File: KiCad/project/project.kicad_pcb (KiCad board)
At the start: 4 copper layers, 26.1 x 21 mm, 20 parts, among them P1 Header-Female-2.54_1x3, U1 DRV8313PWPR

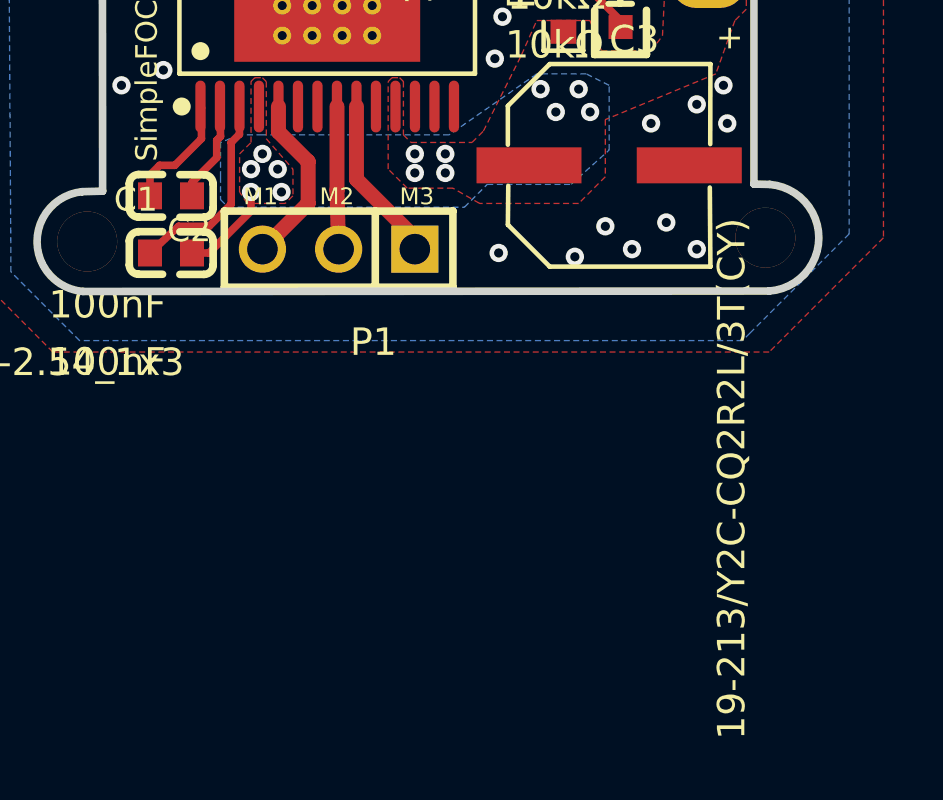
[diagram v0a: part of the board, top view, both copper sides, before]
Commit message: PCB: add C5 footprint, widen VM trace to 0.8mm
- Added C5 (clone of C3, netted VCC/GND), parked below the board outline
  pending placement (shows as 2 ratsnest until routed).
- Widened the VM/VCC trace 0.254 -> 0.8mm (Power-class). No shorts.
- Phase traces left at 0.5mm: widening to 0.8mm shorts U1_8<->U1_9 at the
  0.65mm-pitch HTSSOP escape (they must neck at the IC, a routing task).
  0.5mm carries 1.5A.

DRC: 0 shorting_items, 2 unconnected (C5's pads). Remaining are
pre-existing import artifacts. Footprint resizes + P1 terminal block +
routing belong to the re-layout (they need the larger board).

Co-Authored-By: Claude Opus 4.8 <noreply@anthropic.com>
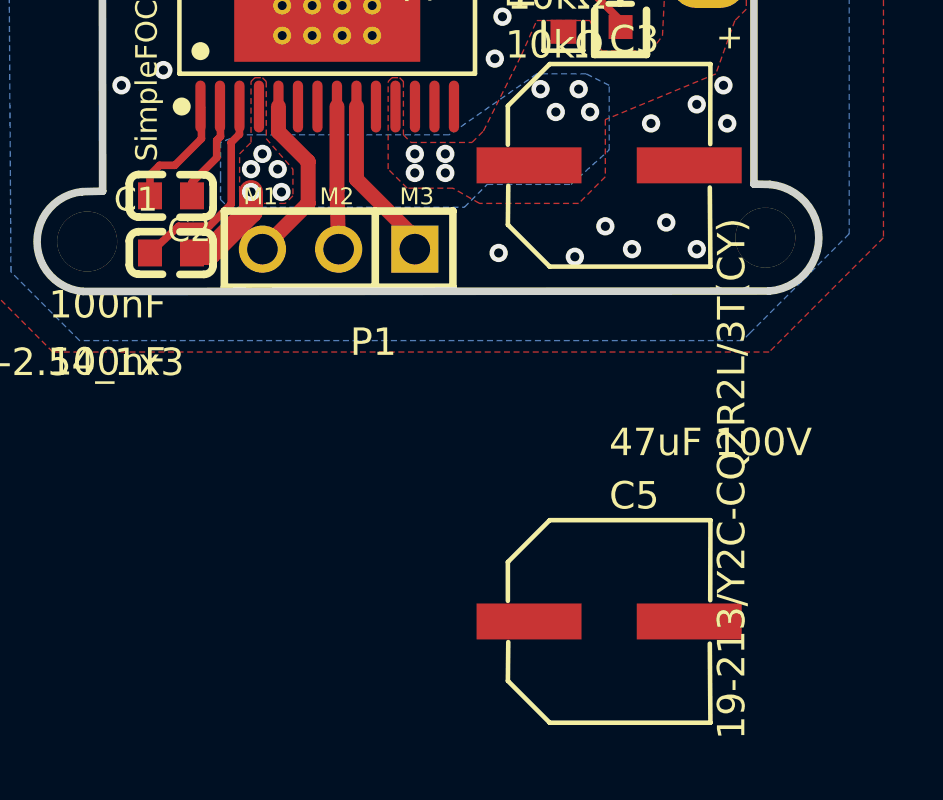
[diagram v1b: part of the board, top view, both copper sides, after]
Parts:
- added C5: 47uF 100V, CAP-SMD_BD6.3-L6.6-W6.6-FD, F.Cu at (153.0, 124.0)

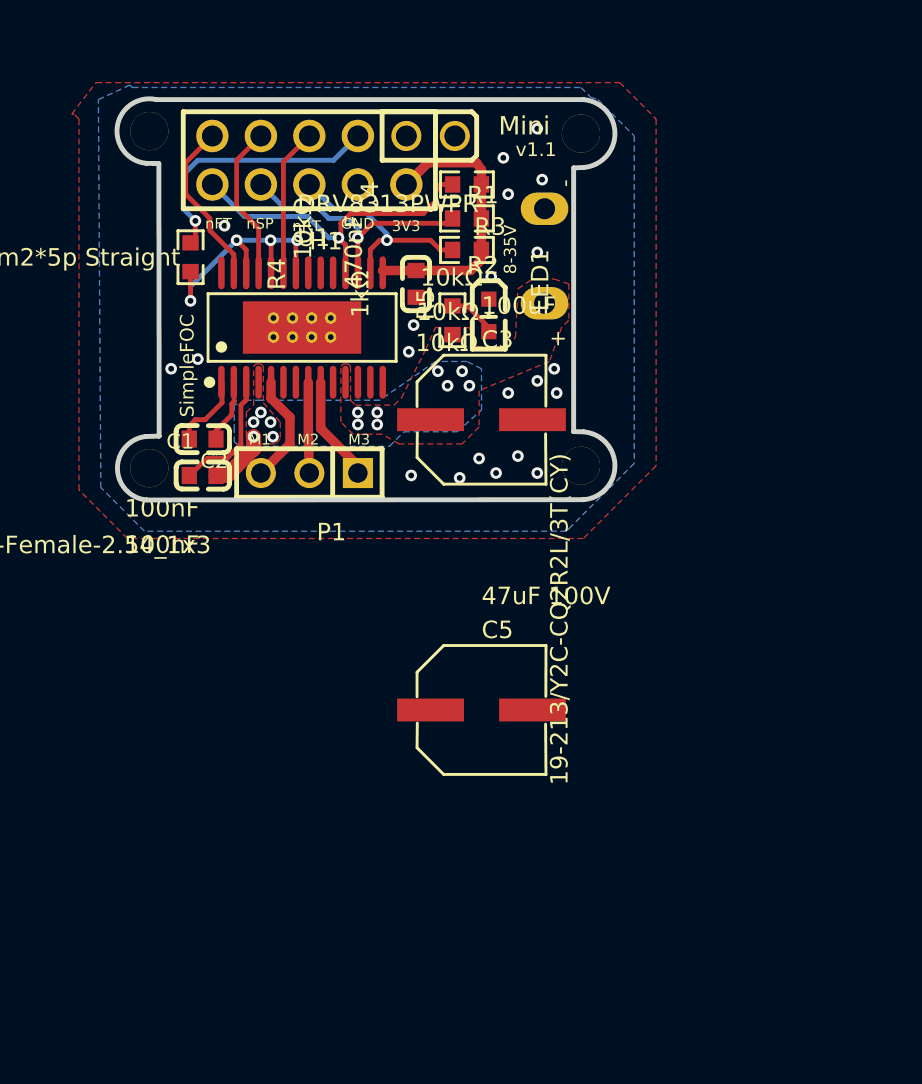
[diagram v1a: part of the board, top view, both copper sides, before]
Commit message: PCB: round corners, add M3 corner holes + missing TB_PWR1 footprint
Continuing the 40x40 mm re-layout (step 1):
- Edge.Cuts: 3 mm rounded corners (4 segments + 4 fillet arcs).
- Add MH1-MH4 (MountingHole_3.2mm_M3, NPTH) at the corners, symmetric
  32x32 mm pattern (4 mm inset). MH1 overlaps H1 until H1 is moved.
- Add TB_PWR1 footprint (was in the schematic but the import never laid
  it out): TerminalBlock_MaiXu_MX126-5.0-02P, pad1->GND, pad2->VCC,
  parked off-board pending placement.
- Re-pour zones after the edge change (clears stale-fill edge flags).

DRC: 228 violations, 0 shorting_items, 4 unconnected (C5 + TB_PWR1).
The 7 Pad_gge* orphans (old 2 mm GND mounting holes + original power
pads) are now superseded by MH1-4 / TB_PWR1 -- flagged in docs for
deletion during GUI placement.

Co-Authored-By: Claude Opus 4.8 (1M context) <noreply@anthropic.com>
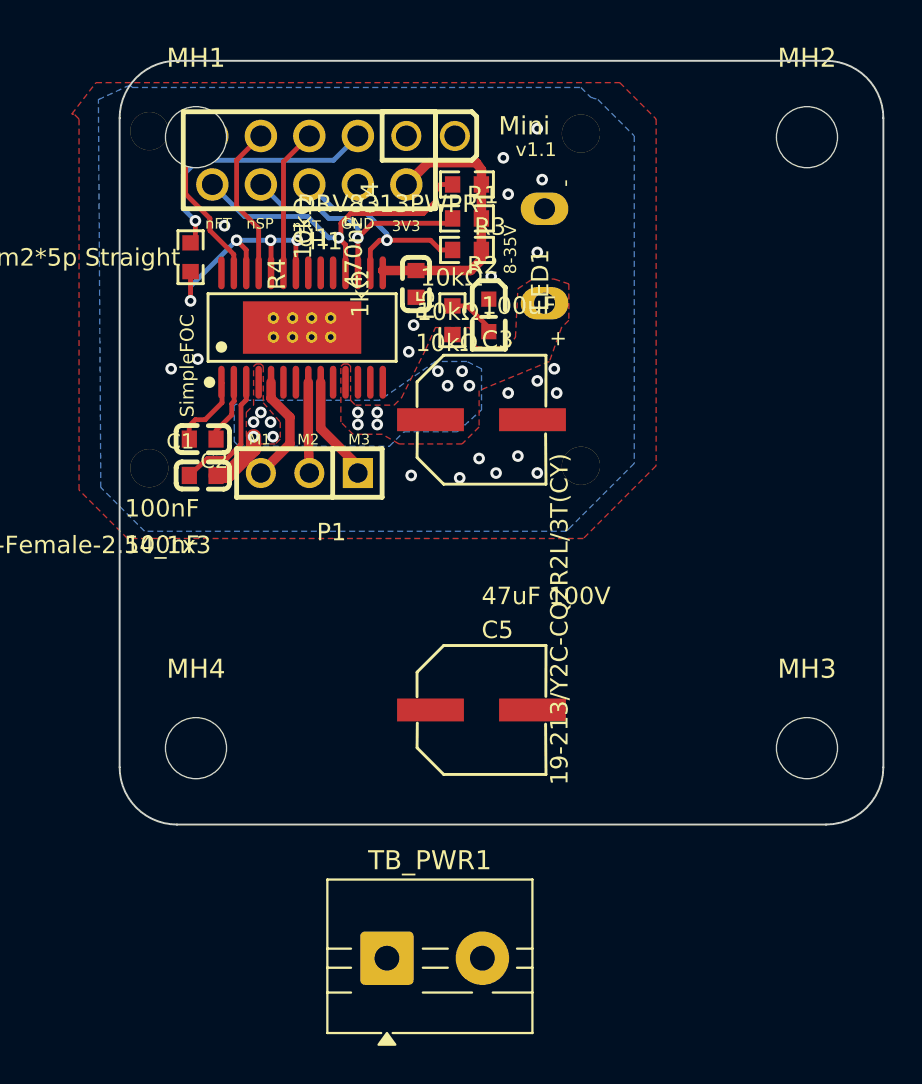
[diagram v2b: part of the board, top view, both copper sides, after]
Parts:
- added MH1: MountingHole_3.2mm_M3, MountingHole_3.2mm_M3, F.Cu at (138.0, 94.0)
- added MH2: MountingHole_3.2mm_M3, MountingHole_3.2mm_M3, F.Cu at (170.0, 94.0)
- added MH3: MountingHole_3.2mm_M3, MountingHole_3.2mm_M3, F.Cu at (170.0, 126.0)
- added MH4: MountingHole_3.2mm_M3, MountingHole_3.2mm_M3, F.Cu at (138.0, 126.0)
- added TB_PWR1: TB002-500-02BE, TerminalBlock_MaiXu_MX126-5.0-02P_1x02_P5.00mm, F.Cu at (148.0, 137.0)
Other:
- board size 26.1 x 21 mm -> 40 x 40 mm

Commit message: PCB: clear routing/zones/orphans for tool-driven re-place + re-route
Hand a clean board to KiCadRoutingTools: removed all 112 tracks + 42 vias,
the 7 Pad_gge import orphans (4 old corner mounting holes + 3 old power-input
pads, both superseded by MH1-MH4 / TB_PWR1), all 7 stale copper zones, and the
Dwgs.User documentation graphics. Kept all real components, MH1-MH4, and the
40x40 Edge.Cuts outline. Planes will be regenerated via route_planes.

Co-Authored-By: Claude Opus 4.8 (1M context) <noreply@anthropic.com>
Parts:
- removed Pad_gge5124: Pad_gge5124, Pad_gge5124
- removed Pad_gge5154: Pad_gge5154, Pad_gge5154
- removed Pad_gge5250: Pad_gge5250, Pad_gge5250
- removed Pad_gge5325: Pad_gge5325, Pad_gge5325
- removed Pad_gge5349: Pad_gge5349, Pad_gge5349
- removed Pad_gge7437: Pad_gge7437, Pad_gge7437
- removed Pad_gge9415: Pad_gge9415, Pad_gge9415
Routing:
- net NFLT: track 17.6 -> 0.00 mm, vias 1 -> 0
- net 3.3V: track 14.7 -> 0.00 mm
- net EN: track 14.3 -> 0.00 mm, vias 4 -> 0
- net R4_1: track 14.1 -> 0.00 mm, vias 1 -> 0
- net NSLP: track 13.8 -> 0.00 mm, vias 1 -> 0
- net NRES: track 11.4 -> 0.00 mm, vias 1 -> 0
- net IN1: track 8.79 -> 0.00 mm
- net U1_25: track 8.17 -> 0.00 mm
- net IN3: track 7.73 -> 0.00 mm
- net U1_3: track 6.73 -> 0.00 mm
- net U1_5: track 5.80 -> 0.00 mm
- net U1_9: track 5.56 -> 0.00 mm
- net U1_8: track 4.76 -> 0.00 mm
- net U1_1: track 4.00 -> 0.00 mm
- net U1_2: track 3.37 -> 0.00 mm
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- removed copper zone on B.Cu, net GND
- removed copper zone on F.Cu, net GND
- removed copper zone on In1.Cu, net GND
- removed copper zone on In2.Cu, net GND
- removed copper zone on B.Cu, net VCC
- removed copper zone on F.Cu, net VCC

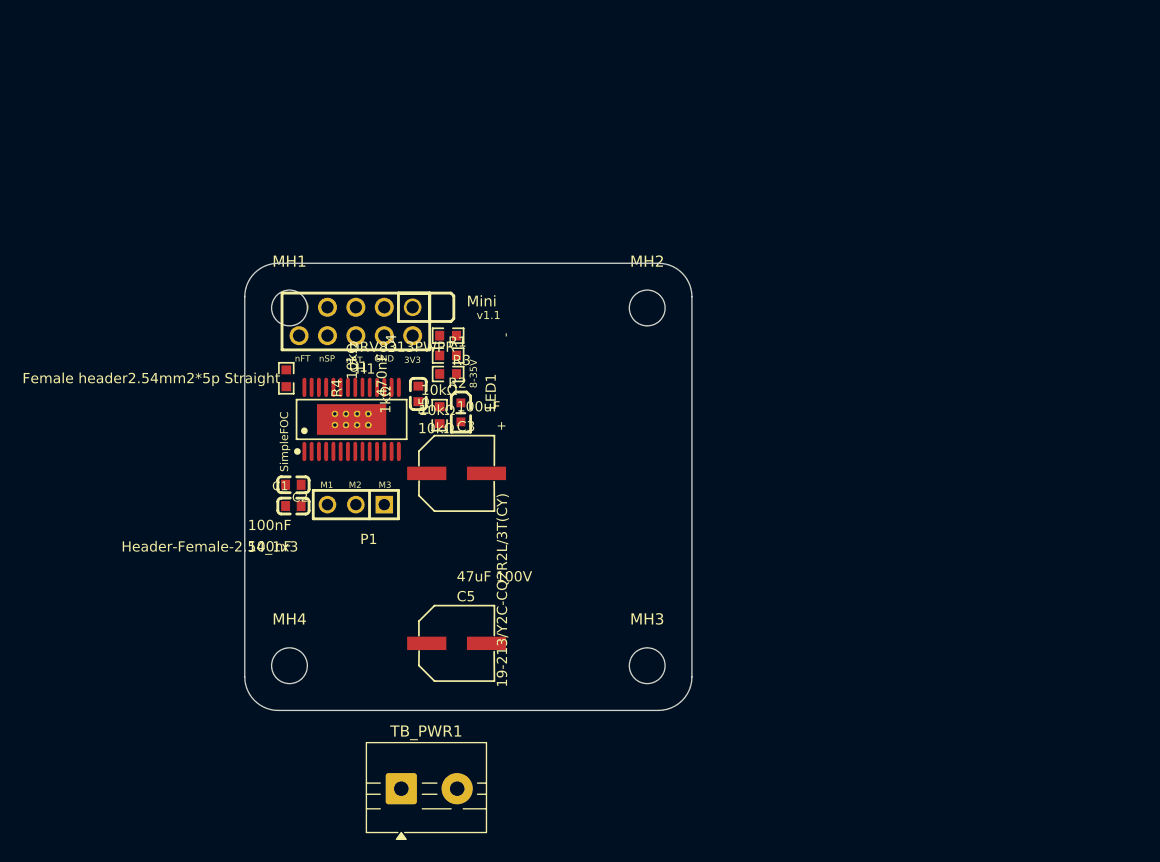
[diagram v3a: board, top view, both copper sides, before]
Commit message: PCB: first-pass macro placement on 40x40 board
Power-in (TB_PWR1) left edge, motor-out (P1) right edge, control header (H1)
top edge facing U1's logic row. U1 central; bulk VM cans in the open bottom
area; CP/bypass caps under the power row; logic pulls between H1 and U1; LED
by the 3.3V pin. 0 courtyard overlaps (remaining DRC = cosmetic silk +
unrouted ratsnest). Starting point for KiCadRoutingTools polish + route.

Co-Authored-By: Claude Opus 4.8 (1M context) <noreply@anthropic.com>
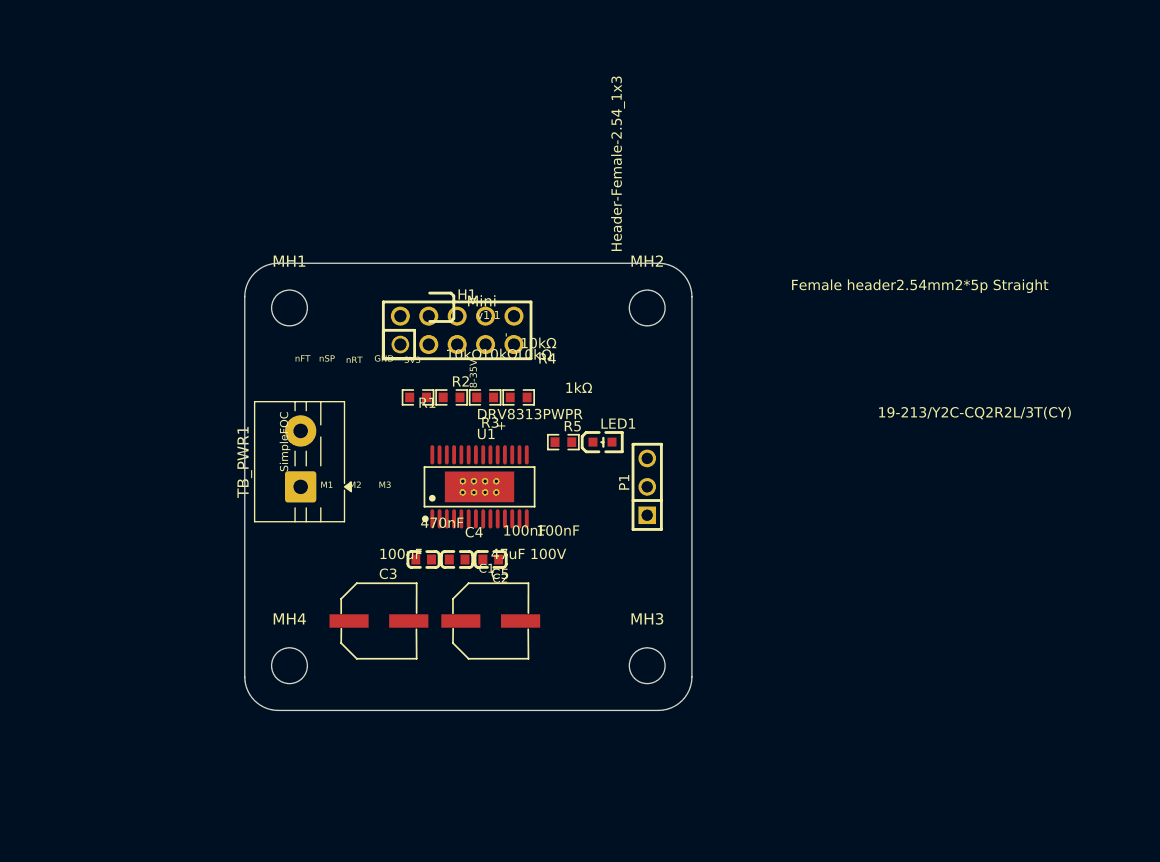
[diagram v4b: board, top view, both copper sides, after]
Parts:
- moved TB_PWR1 28.5 mm to (139.0, 110.0), turned to 90 degrees
- moved P1 26.1 mm to (170.0, 110.0), turned to 90 degrees
- moved R4 20.9 mm to (158.5, 102.0), turned to 0 degrees
- moved C2 18.3 mm to (156.0, 116.5), turned to 0 degrees
- moved C1 16.1 mm to (153.0, 116.5), turned to 0 degrees
- moved C3 14.9 mm to (146.0, 122.0)
- moved C4 14.8 mm to (150.0, 116.5), turned to 0 degrees
- moved LED1 12.9 mm to (166.0, 106.0), turned to 0 degrees
- moved U1 12.9 mm to (155.0, 110.0)
- moved R5 11.3 mm to (162.5, 106.0), turned to 0 degrees
- moved H1 9.10 mm to (153.0, 96.0), turned to 0 degrees
- moved R1 6.14 mm to (149.5, 102.0), turned to 0 degrees
- moved R3 3.92 mm to (155.5, 102.0), turned to 0 degrees
- moved R2 3.76 mm to (152.5, 102.0), turned to 0 degrees
- moved C5 3.64 mm to (156.0, 122.0)

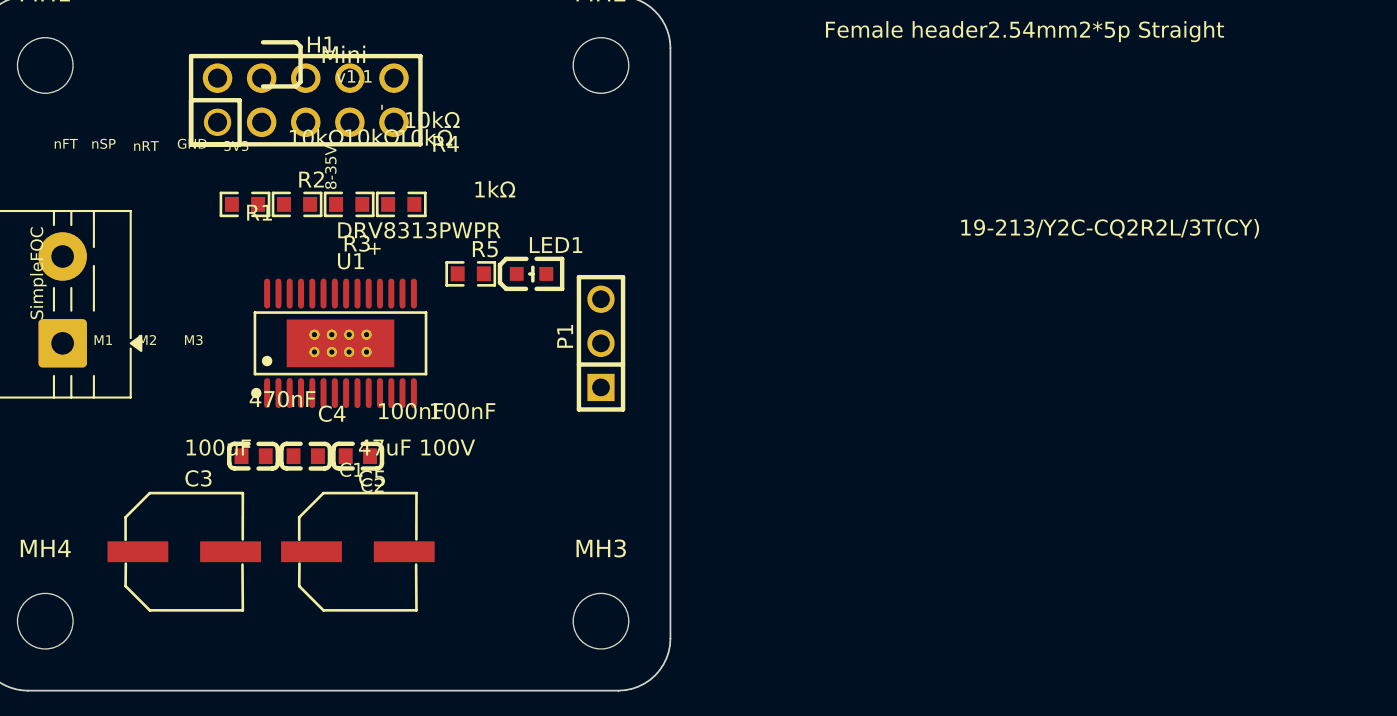
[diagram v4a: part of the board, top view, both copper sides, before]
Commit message: PCB: place_optimize polish of macro placement
KiCadRoutingTools place_optimize (connectors/U1/holes locked): airwire
194.9->179.9mm, crossings 39->19, 10 small parts nudged. Bulk cans manually
reset clear of MH4 afterward. 0 courtyard overlaps. Writer verified to
preserve the 4-layer stackup (GND1/GND2 inner names intact), 19 footprints,
20 nets.

Co-Authored-By: Claude Opus 4.8 (1M context) <noreply@anthropic.com>
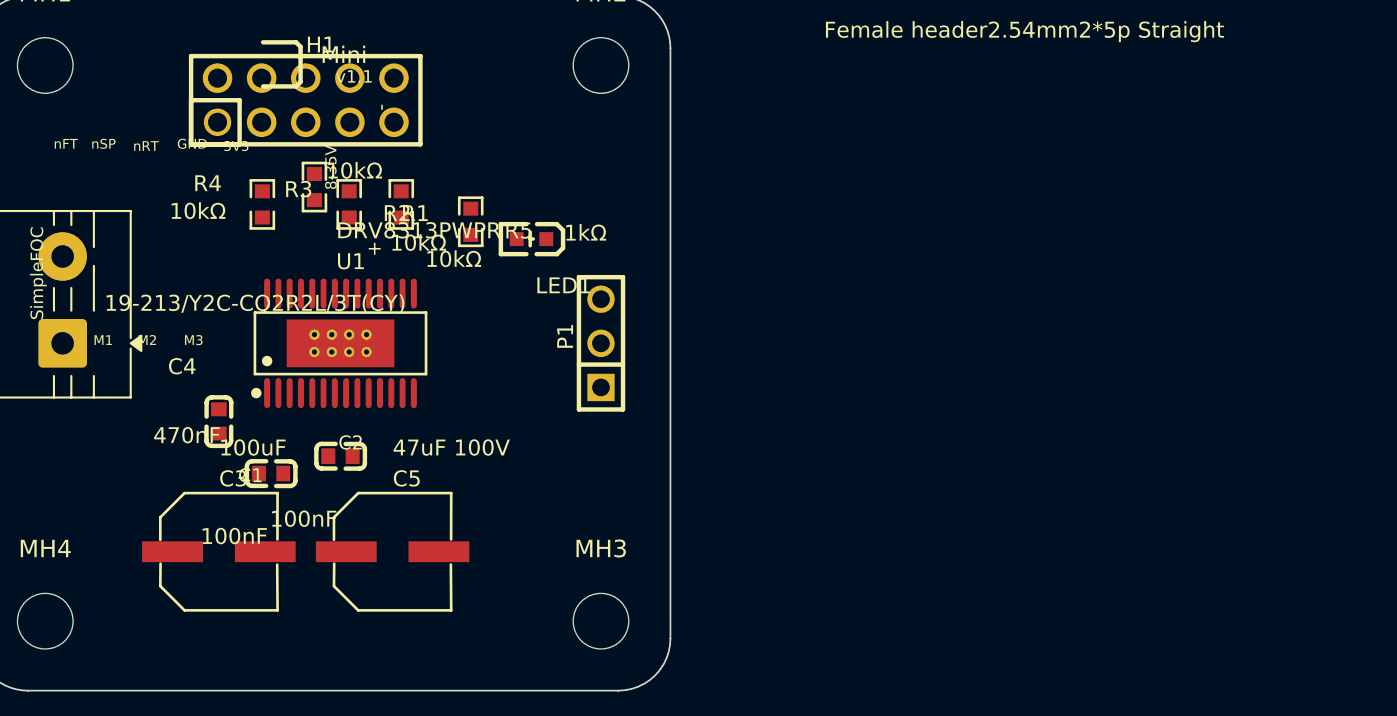
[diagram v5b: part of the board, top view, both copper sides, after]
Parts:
- moved R1 9.00 mm to (158.5, 102.0), turned to 90 degrees
- moved R4 8.00 mm to (150.5, 102.0), turned to 90 degrees
- moved R2 3.00 mm to (155.5, 102.0), turned to -90 degrees
- moved R5 3.00 mm to (162.5, 103.0), turned to -90 degrees
- moved C4 2.83 mm to (148.0, 114.5), turned to 90 degrees
- moved C1 2.24 mm to (151.0, 117.5), turned to 180 degrees
- moved R3 2.24 mm to (153.5, 101.0), turned to -90 degrees
- moved C3 2.00 mm to (148.0, 122.0)
- moved C5 2.00 mm to (158.0, 122.0)
- moved LED1 2.00 mm to (166.0, 104.0), turned to 180 degrees
- moved C2 1.00 mm to (155.0, 116.5), turned to 180 degrees
